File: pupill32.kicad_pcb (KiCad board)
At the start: 2 copper layers, 52.1 x 27.9 mm, 54 parts, among them J1 HeaderR, J2 HeaderL, J3 USB_PINS, J4 SWD_HEADER, SW1 RST_BTN, SW2 BOOT_BTN, U1 SRV05-4, U2 PY32F030F18P6, U3 CH340N, U4 AMS1117-3.3, Y1 32.768 kHz, Y2 12M

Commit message: bot silks
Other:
- board text added: "Open HW: CERN- OHL-W"
- board text added: "PU(RPLE) PILL32 for"
- board text added: "rev.B"
- board text removed: "LICENSE: CERN- OHL-W"
- board text removed: "PCB rev.B"
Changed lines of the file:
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@@
 		)
 	)
-	(gr_text "PCB\nrev.B"
-		(at 104.2416 82.8548 0)
-		(layer "B.SilkS")
-		(effects
-			(font
-				(size 1.5 1.5)
+	(gr_text "rev.B"
+		(at 104.394 81.9404 0)
+		(layer "B.SilkS")
+		(effects
+			(font
+				(size 1.8 1.5)
 				(thickness 0.375)
 				(bold yes)
@@
 		)
 	)
+	(gr_text "PU(RPLE)\nPILL32 for"
+		(at 129.6416 77.724 0)
+		(layer "B.SilkS")
+		(effects
+			(font
+				(size 1.5 1.2)
+				(thickness 0.3)
+				(bold yes)
+			)
+			(justify left bottom mirror)
+		)
+	)
 	(gr_text "SWD"
 		(at 122.5042 69.9262 0)
@@
 	)
 	(gr_text "PY32F030\nF18P6"
-		(at 131.2672 83.2104 0)
+		(at 131.0132 83.058 0)
 		(layer "B.SilkS")
 		(effects
@@
 		)
 	)
-	(gr_text "LICENSE:\nCERN-\nOHL-W"
+	(gr_text "Open HW:\nCERN-\nOHL-W"
 		(at 109.5502 78.7654 0)
 		(layer "B.SilkS")

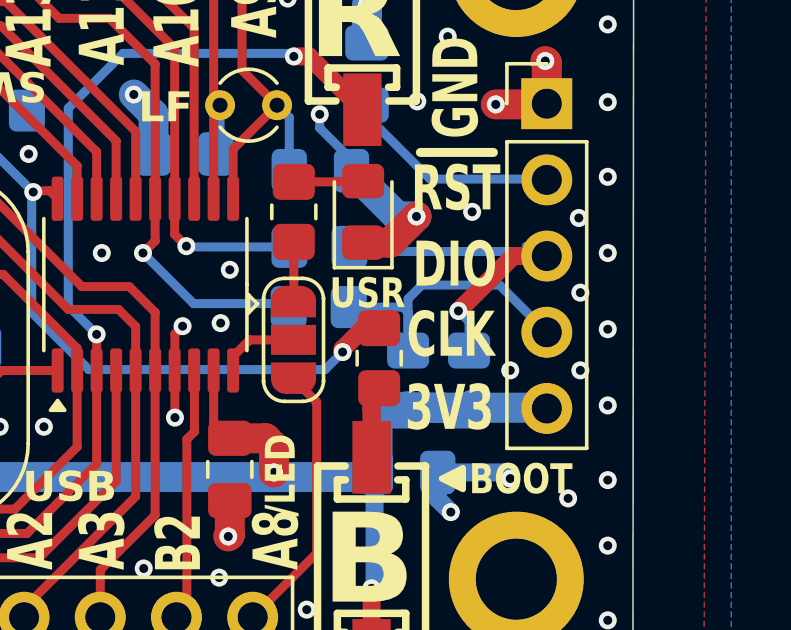
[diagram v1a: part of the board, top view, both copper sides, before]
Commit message: SWCLK pulled down (corrected)
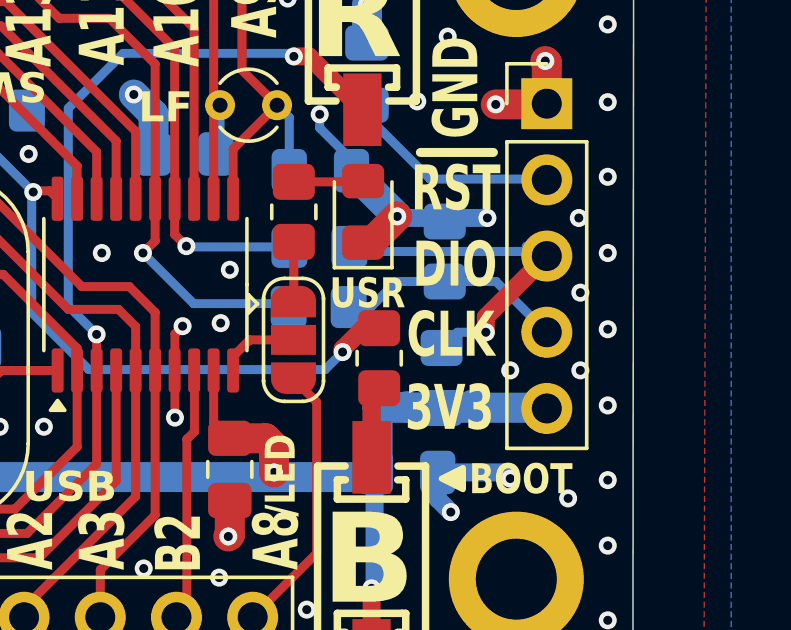
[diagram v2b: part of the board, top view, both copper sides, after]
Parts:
- moved R11 4.47 mm to (135.9, 75.4), turned to 90 degrees
- moved R12 0.92 mm to (135.8, 79.7)
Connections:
- R11 pad 2: +3V3 -> GND
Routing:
- net SWDCLK: track 10.5 -> 7.66 mm
- net GND: track 128.5 -> 130.2 mm
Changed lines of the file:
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@@
 	(footprint "Resistor_SMD:R_0805_2012Metric_Pad1.20x1.40mm_HandSolder"
 		(layer "B.Cu")
-		(at 136.7536 79.74 -90)
+		(at 135.8392 79.6544 -90)
 		(descr "Resistor SMD 0805 (2012 Metric), square (rectangular) end terminal, IPC_7351 nominal with elongated pad for handsoldering. (Body size source: IPC-SM-782 page 72, https://www.pcb-3d.com/wordpress/wp-content/uploads/ipc-sm-782a_amendment_1_and_2.pdf), generated with kicad-footprint-generator")
 		(tags "resistor handsolder")
@@
 		(tags "resistor handsolder")
 		(property "Reference" "R9"
-			(at 0 1.65 360)
+			(at 0 1.65 0)
 			(layer "B.SilkS")
 			(hide yes)
@@
 		)
 		(property "Value" "22R"
-			(at 0 -1.65 360)
+			(at 0 -1.65 0)
 			(layer "B.Fab")
 			(effects
@@
 		)
 		(fp_text user "${REFERENCE}"
-			(at 0 0 360)
+			(at 0 0 0)
 			(layer "B.Fab")
 			(effects
@@
 	(footprint "Resistor_SMD:R_0805_2012Metric_Pad1.20x1.40mm_HandSolder"
 		(layer "B.Cu")
-		(at 134.7216 79.74 -90)
+		(at 135.9408 75.438 90)
 		(descr "Resistor SMD 0805 (2012 Metric), square (rectangular) end terminal, IPC_7351 nominal with elongated pad for handsoldering. (Body size source: IPC-SM-782 page 72, https://www.pcb-3d.com/wordpress/wp-content/uploads/ipc-sm-782a_amendment_1_and_2.pdf), generated with kicad-footprint-generator")
 		(tags "resistor handsolder")
@@
 		)
 		(property "Footprint" "Resistor_SMD:R_0805_2012Metric_Pad1.20x1.40mm_HandSolder"
-			(at 0 0 90)
+			(at 0 0 -90)
 			(unlocked yes)
 			(layer "B.Fab")
@@
 		)
 		(property "Datasheet" ""
-			(at 0 0 90)
+			(at 0 0 -90)
 			(unlocked yes)
 			(layer "B.Fab")
@@
 		)
 		(property "Description" ""
-			(at 0 0 90)
+			(at 0 0 -90)
 			(unlocked yes)
 			(layer "B.Fab")
@@
 		(attr smd)
 		(fp_line
-			(start 0.227064 0.735)
-			(end -0.227064 0.735)
+			(start 0.227064 -0.735)
+			(end -0.227064 -0.735)
 			(stroke
 				(width 0.12)
@@
 		)
 		(fp_line
-			(start 0.227064 -0.735)
-			(end -0.227064 -0.735)
+			(start 0.227064 0.735)
+			(end -0.227064 0.735)
 			(stroke
 				(width 0.12)
@@
 		)
 		(fp_line
-			(start -1.85 0.95)
-			(end -1.85 -0.95)
+			(start 1.85 -0.95)
+			(end 1.85 0.95)
 			(stroke
 				(width 0.05)
@@
 		)
 		(fp_line
-			(start 1.85 0.95)
-			(end -1.85 0.95)
+			(start -1.85 -0.95)
+			(end 1.85 -0.95)
 			(stroke
 				(width 0.05)
@@
 		)
 		(fp_line
-			(start -1.85 -0.95)
-			(end 1.85 -0.95)
+			(start 1.85 0.95)
+			(end -1.85 0.95)
 			(stroke
 				(width 0.05)
@@
 		)
 		(fp_line
-			(start 1.85 -0.95)
-			(end 1.85 0.95)
+			(start -1.85 0.95)
+			(end -1.85 -0.95)
 			(stroke
 				(width 0.05)
@@
 		)
 		(fp_line
-			(start -1 0.625)
-			(end -1 -0.625)
+			(start 1 -0.625)
+			(end 1 0.625)
 			(stroke
 				(width 0.1)
@@
 		)
 		(fp_line
-			(start 1 0.625)
-			(end -1 0.625)
+			(start -1 -0.625)
+			(end 1 -0.625)
 			(stroke
 				(width 0.1)
@@
 		)
 		(fp_line
-			(start -1 -0.625)
-			(end 1 -0.625)
+			(start 1 0.625)
+			(end -1 0.625)
 			(stroke
 				(width 0.1)
@@
 		)
 		(fp_line
-			(start 1 -0.625)
-			(end 1 0.625)
+			(start -1 0.625)
+			(end -1 -0.625)
 			(stroke
 				(width 0.1)
@@
 		)
 		(pad "1" smd roundrect
-			(at -1 0 270)
+			(at -1 0 90)
 			(size 1.2 1.4)
 			(layers "B.Cu" "B.Paste" "B.Mask")
@@
 		)
 		(pad "2" smd roundrect
-			(at 1 0 270)
+			(at 1 0 90)
 			(size 1.2 1.4)
 			(layers "B.Cu" "B.Paste" "B.Mask")
 			(roundrect_rratio 0.208333)
-			(net 13 "+3V3")
+			(net 3 "GND")
 			(pintype "passive")
 		)
@@
 		)
 		(property "Value" "22R"
-			(at 0 -1.65 360)
+			(at 0 -1.65 0)
 			(layer "B.Fab")
 			(effects
@@
 		)
 		(fp_text user "${REFERENCE}"
-			(at 0 0 360)
+			(at 0 0 0)
 			(layer "B.Fab")
 			(effects
@@
 	)
 	(segment
-		(start 135 74.2696)
-		(end 134.1274 75.1422)
+		(start 134.3582 74.2696)
+		(end 133.4856 75.1422)
 		(width 1)
 		(layer "F.Cu")
@@
 	)
 	(segment
-		(start 134.1274 75.1422)
-		(end 133.223 75.1422)
-		(width 1)
-		(layer "F.Cu")
-		(net 3)
-	)
-	(segment
 		(start 110.5066 75.2348)
 		(end 109.304 75.2348)
@@
 	)
 	(segment
+		(start 133.4856 75.1422)
+		(end 133.223 75.1422)
+		(width 1)
+		(layer "F.Cu")
+		(net 3)
+	)
+	(segment
 		(start 91.44 73.66)
 		(end 91.44 77.47)
@@
 	)
 	(via
-		(at 135 74.2696)
+		(at 134.3582 74.2696)
 		(size 0.6)
 		(drill 0.3)
@@
 	)
 	(via
-		(at 136.8552 74.1172)
+		(at 137.3632 74.3204)
 		(size 0.6)
 		(drill 0.3)
@@
 	)
 	(segment
-		(start 135 74.2696)
-		(end 134.3582 74.2696)
-		(width 1)
-		(layer "B.Cu")
-		(net 3)
-	)
-	(segment
 		(start 111.0654 71.8146)
 		(end 111.8401 71.0399)
@@
 	)
 	(segment
+		(start 137.3632 74.3204)
+		(end 134.409 74.3204)
+		(width 0.6)
+		(layer "B.Cu")
+		(net 3)
+	)
+	(segment
 		(start 104.0091 70.4811)
 		(end 103.7844 70.2564)
@@
 	)
 	(segment
+		(start 134.3582 74.2696)
+		(end 132.8342 72.7456)
+		(width 1)
+		(layer "B.Cu")
+		(net 3)
+	)
+	(segment
 		(start 91.76 70.17)
 		(end 91.44 69.85)
@@
 	)
 	(segment
-		(start 134.3582 74.2696)
-		(end 132.8342 72.7456)
-		(width 1)
-		(layer "B.Cu")
-		(net 3)
-	)
-	(segment
 		(start 133.35 68.4862)
 		(end 133.35 67.2084)
@@
 	)
 	(segment
+		(start 134.409 74.3204)
+		(end 134.3582 74.2696)
+		(width 0.6)
+		(layer "B.Cu")
+		(net 3)
+	)
+	(segment
 		(start 95.0976 77.5716)
 		(end 95.0976 77.639608)
@@
 	)
 	(segment
-		(start 135.1788 76.5556)
-		(end 137.7696 76.5556)
+		(start 134.3312 76.438)
+		(end 135.9408 76.438)
 		(width 0.3)
 		(layer "B.Cu")
@@
 	)
 	(segment
-		(start 137.7696 76.5556)
+		(start 137.652 76.438)
 		(end 139.3444 78.1304)
 		(width 0.3)
@@
 	)
 	(segment
-		(start 134.5438 77.2922)
-		(end 134.7216 77.47)
-		(width 0.3)
-		(layer "B.Cu")
-		(net 29)
-	)
-	(segment
-		(start 134.7216 78.74)
-		(end 134.7216 77.0128)
-		(width 0.3)
-		(layer "B.Cu")
-		(net 29)
-	)
-	(segment
-		(start 134.7216 77.47)
-		(end 134.7216 78.74)
+		(start 132.7404 77.2922)
+		(end 133.477 77.2922)
 		(width 0.3)
 		(layer "B.Cu")
@@
 	)
 	(segment
-		(start 132.7404 77.2922)
-		(end 134.5438 77.2922)
+		(start 135.9408 76.438)
+		(end 137.652 76.438)
 		(width 0.3)
 		(layer "B.Cu")
@@
 	)
 	(segment
-		(start 134.7216 77.0128)
-		(end 135.1788 76.5556)
+		(start 133.477 77.2922)
+		(end 134.3312 76.438)
 		(width 0.3)
 		(layer "B.Cu")
@@
 	)
 	(segment
-		(start 138.2268 75.5904)
-		(end 136.398 77.4192)
+		(start 137.3124 77.6224)
+		(end 139.3444 75.5904)
 		(width 0.6)
 		(layer "F.Cu")
@@
 	)
 	(segment
-		(start 139.3444 75.5904)
-		(end 138.2268 75.5904)
+		(start 137.3124 78.1304)
+		(end 137.3124 77.6224)
 		(width 0.6)
 		(layer "F.Cu")
@@
 	)
 	(via
-		(at 136.398 77.4192)
+		(at 137.3124 78.1304)
 		(size 0.6)
 		(drill 0.3)
@@
 	)
 	(segment
-		(start 136.7536 77.7748)
-		(end 136.398 77.4192)
+		(start 138.6586 75.2602)
+		(end 138.9634 75.565)
 		(width 0.3)
 		(layer "B.Cu")
@@
 	)
 	(segment
-		(start 136.7536 78.74)
-		(end 136.7536 77.7748)
+		(start 132.7658 75.2856)
+		(end 132.9182 75.438)
 		(width 0.3)
 		(layer "B.Cu")
@@
 	)
 	(segment
-		(start 138.6586 75.2602)
-		(end 138.9634 75.565)
+		(start 136.3632 78.1304)
+		(end 135.8392 78.6544)
 		(width 0.3)
 		(layer "B.Cu")
@@
 	)
 	(segment
-		(start 132.7658 75.2856)
-		(end 132.9182 75.438)
+		(start 137.3124 78.1304)
+		(end 136.3632 78.1304)
 		(width 0.3)
 		(layer "B.Cu")
